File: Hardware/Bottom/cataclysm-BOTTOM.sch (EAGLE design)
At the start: 37 parts, among them U4 PCF8523

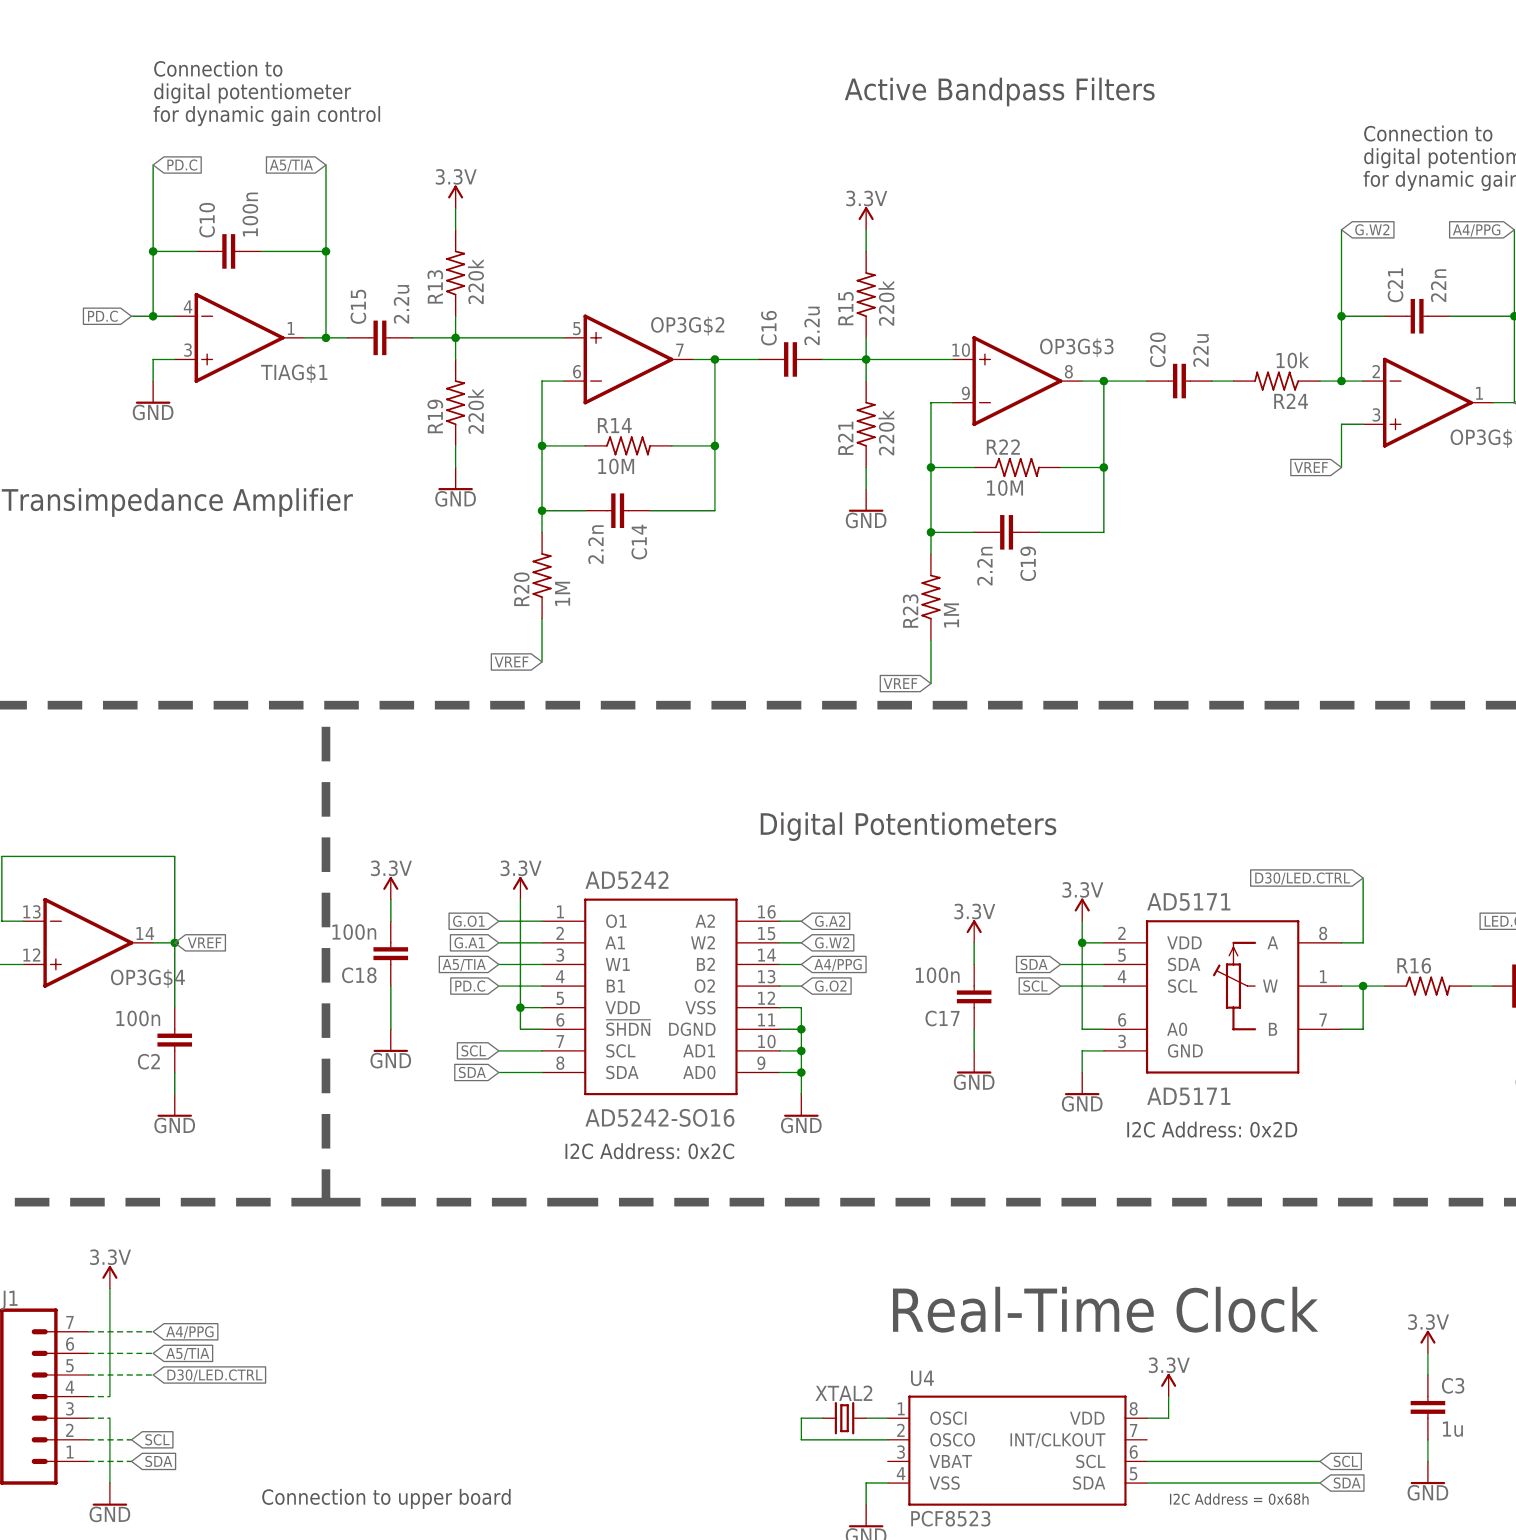
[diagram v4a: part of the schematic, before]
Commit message: Fixed connection b/w top and bottom boards
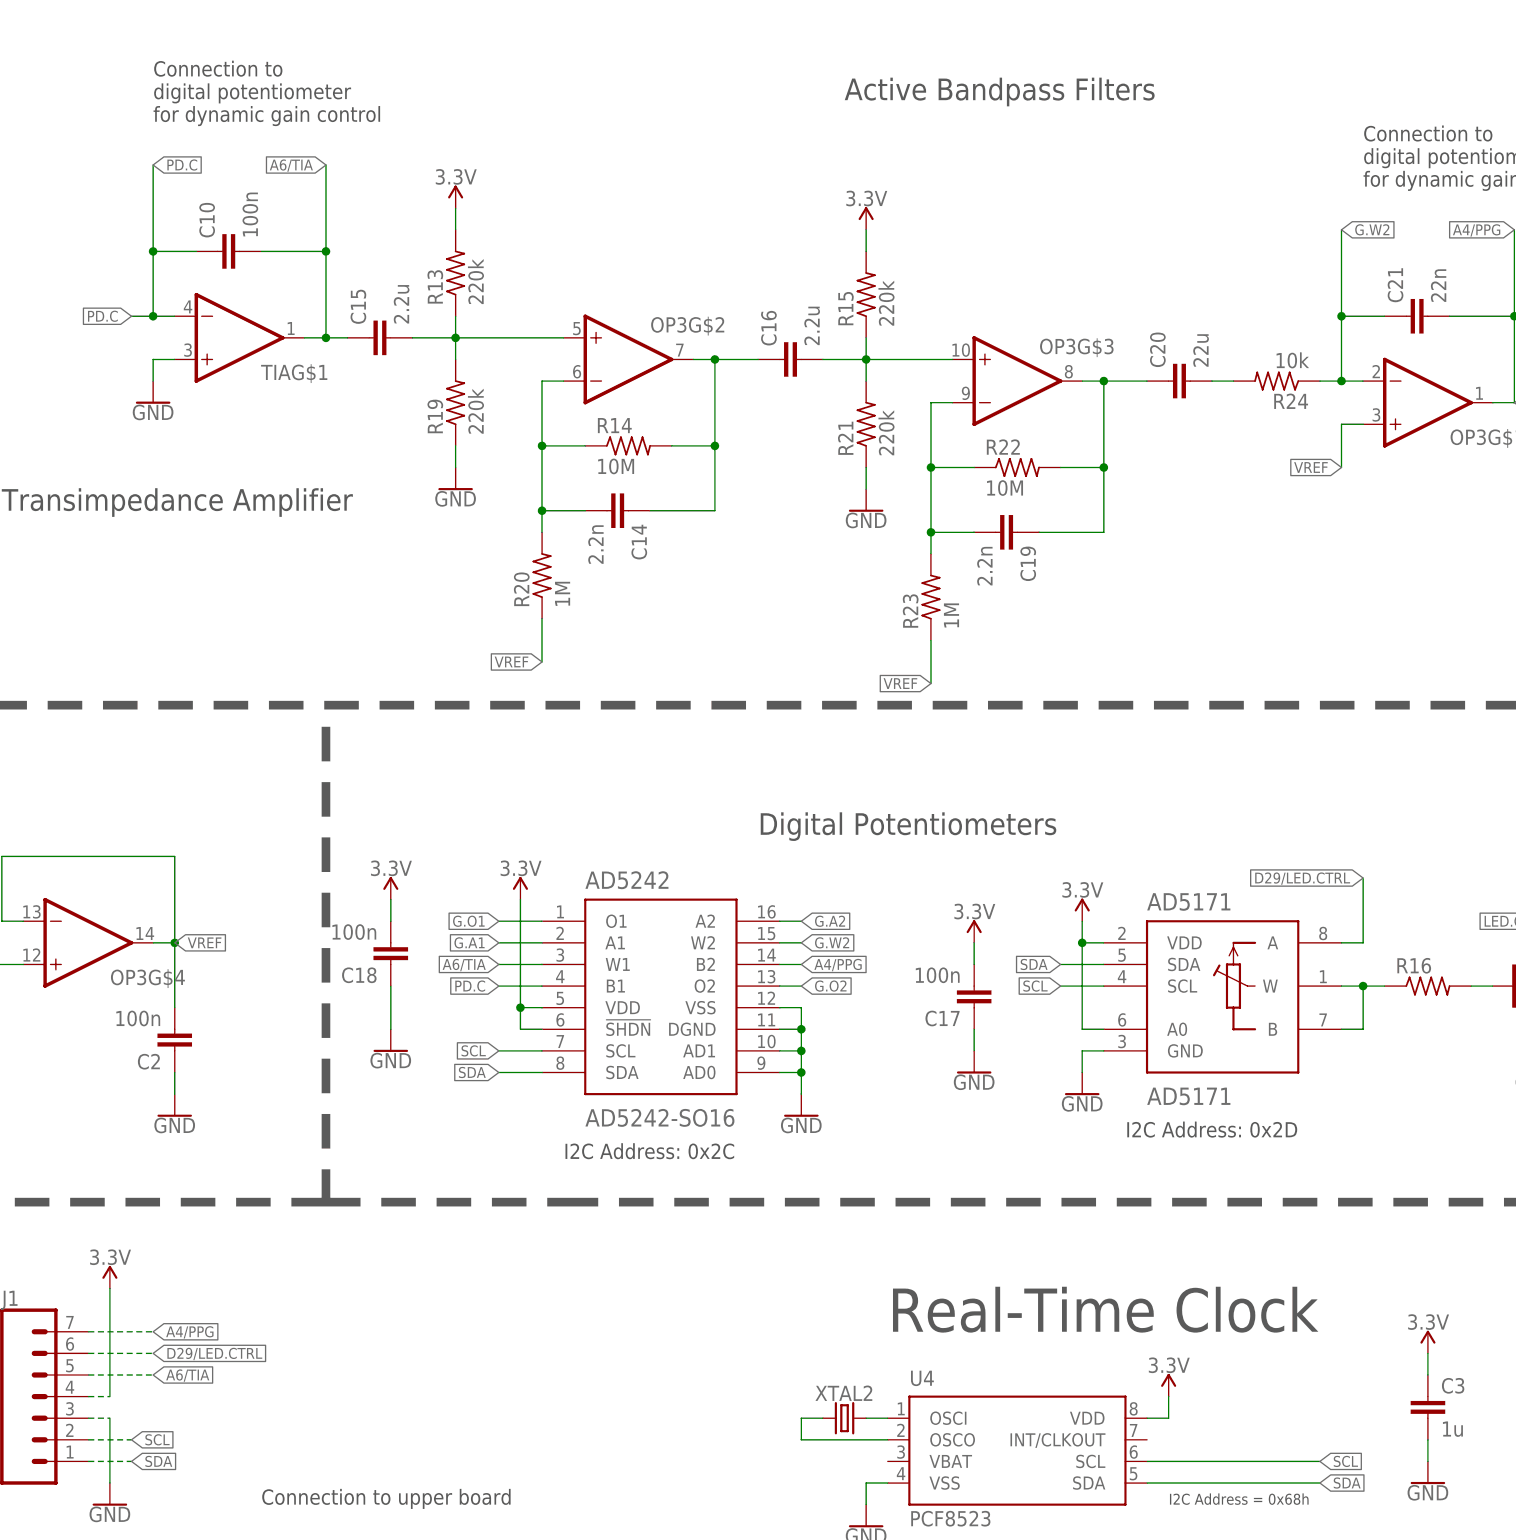
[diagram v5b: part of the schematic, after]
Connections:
- removed net A5/TIA: AD5242.W1, C10.2, C15.1, J1.6, TIAG$1.OUT
- removed net D30/LED.CTRL: AD5171.A, J1.5
- new net A6/TIA: AD5242.W1, C10.2, C15.1, J1.5, TIAG$1.OUT
- new net D29/LED.CTRL: AD5171.A, J1.6
